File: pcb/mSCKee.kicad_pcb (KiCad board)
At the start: 4 copper layers, 275.3 x 124.4 mm, 192 parts, among them IC1 PCA9956BTWY, IC2 PCA9956BTWY, J2 4P4C, J3 4P4C, J4 USB_C_Receptacle_USB2.0_16P, SW1 SW_Push_45deg, SW10 SW_Push_45deg, SW11 SW_Push_45deg, SW12 SW_Push_45deg, SW13 SW_Push_45deg, SW14 SW_Push_45deg, SW15 SW_Push_45deg, SW16 SW_Push_45deg, SW17 SW_Push_45deg, SW18 SW_Push_45deg, SW19 SW_Push_45deg, SW2 SW_Push_45deg, SW20 SW_Push_45deg, SW21 SW_Push_45deg, SW22 SW_Push_45deg, SW23 SW_Push_45deg, SW24 SW_Push_45deg, SW25 SW_Push_45deg, SW26 SW_Push_45deg, SW27 SW_Push_45deg, SW28 SW_Push_45deg, SW29 SW_Push_45deg, SW3 SW_Push_45deg, SW30 SW_Push_45deg, SW31 SW_Push_45deg, SW32 SW_Push_45deg, SW33 SW_Push_45deg, SW34 SW_Push_45deg, SW35 SW_Push_45deg, SW36 SW_Push_45deg, SW4 SW_Push_45deg, SW5 SW_Push_45deg, SW6 SW_Push_45deg, SW7 SW_Push_45deg, SW8 SW_Push_45deg, SW9 SW_Push_45deg, U1 W25Q128JVSIQ, U2 RP2040, U3 NCP1117LPST33T3G, U4 OPT3001DNPR, U5 NCP1117LPST33T3G, U6 MCP23017T-E/ML, U7 OPT3001DNPR, Y1 ABM8-272-T3

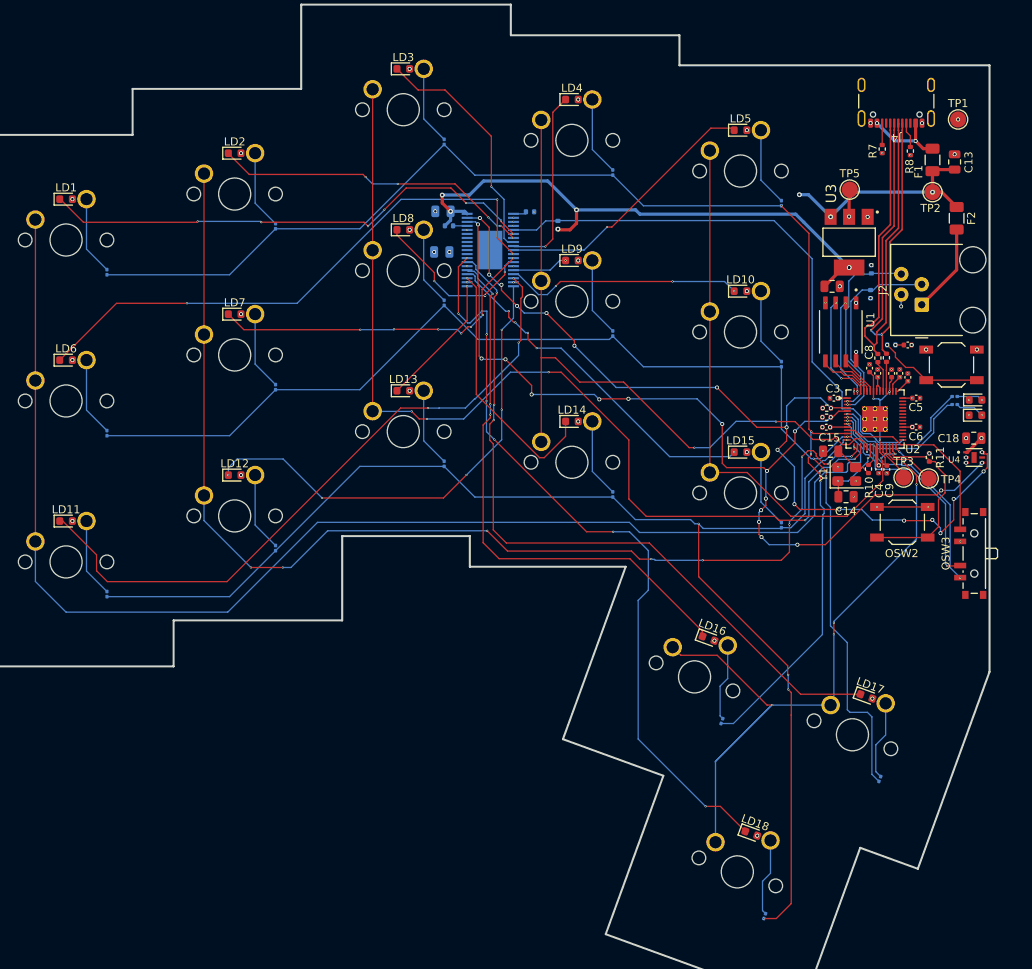
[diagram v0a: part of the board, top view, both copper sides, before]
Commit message: fix: Set all vias to netclass size, fix about half of DRC violations
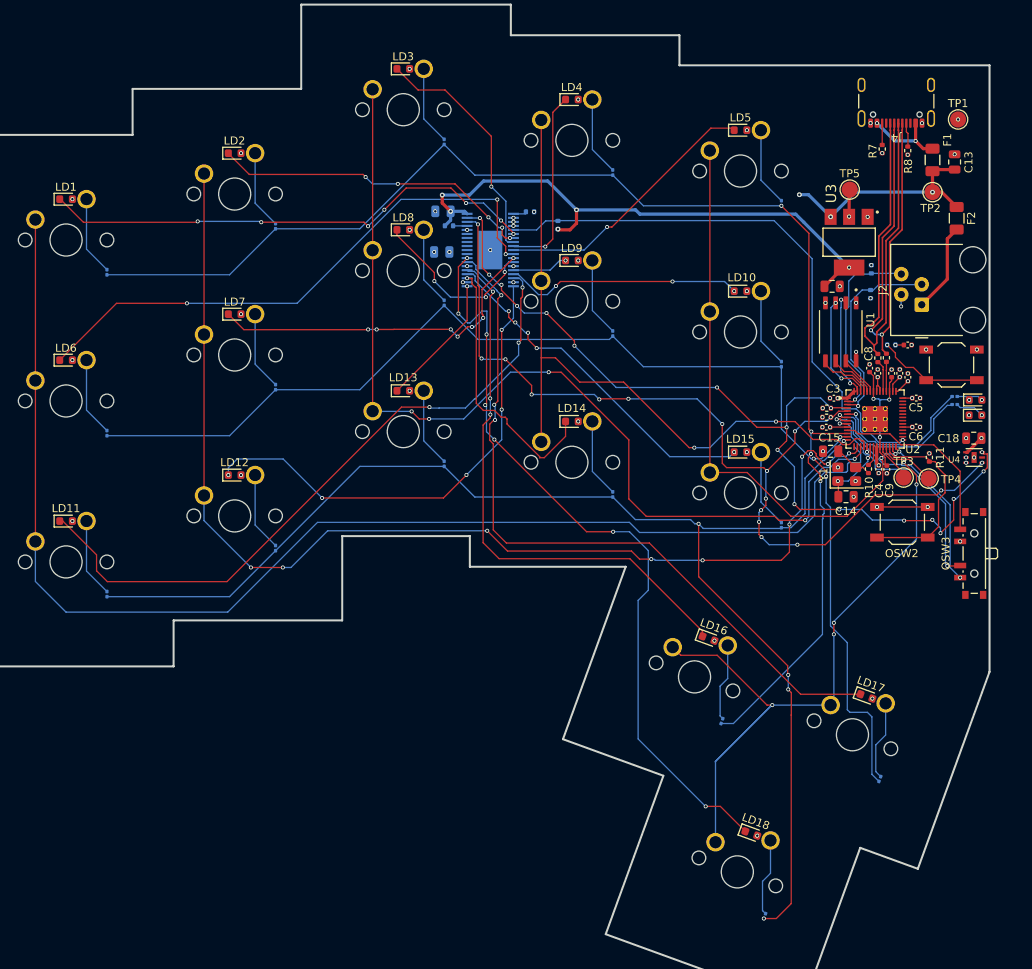
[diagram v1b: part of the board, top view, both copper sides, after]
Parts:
- moved R8 0.33 mm to (188.4, 85.1)
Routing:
- net BL_DIM_1: track 27.5 -> 30.4 mm
- net STATUS2: track 18.7 -> 20.8 mm
- net BL_DIM_2: track 27.5 -> 29.1 mm
- net Net-(IC1-LED13): track 32.2 -> 33.7 mm
- net +3V3: track 94.6 -> 95.7 mm, vias 25 -> 23
- net /master_side/QSPI_SD1: track 12.1 -> 13.3 mm
- net Net-(U2-VREG_VOUT): track 16.4 -> 17.2 mm
- net Net-(IC1-LED16): track 89.8 -> 90.5 mm
- net Net-(IC1-LED6): track 42.4 -> 43.0 mm
- net Net-(IC1-LED5): track 70.3 -> 70.9 mm
- net Net-(IC1-LED10): track 83.2 -> 83.7 mm
- net GND: track 8.45 -> 8.98 mm, vias 48 -> 50
- net Net-(IC1-LED1): track 39.8 -> 40.4 mm
- net Net-(IC1-LED7): track 21.3 -> 21.7 mm, vias 4 -> 3
- net COL0: vias 1 -> 0

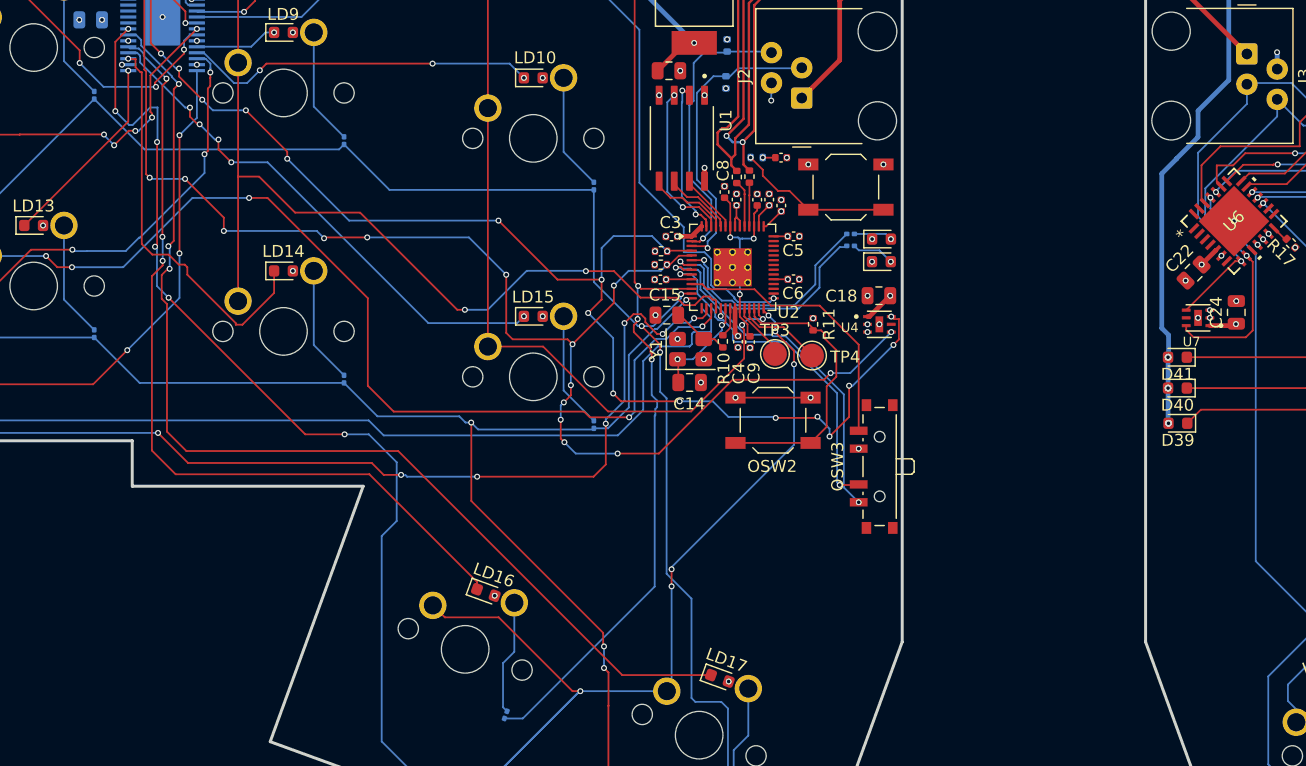
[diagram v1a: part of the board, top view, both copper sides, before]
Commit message: fix: DRC violations, 0 errors, about 70 silkscreen warnings remain
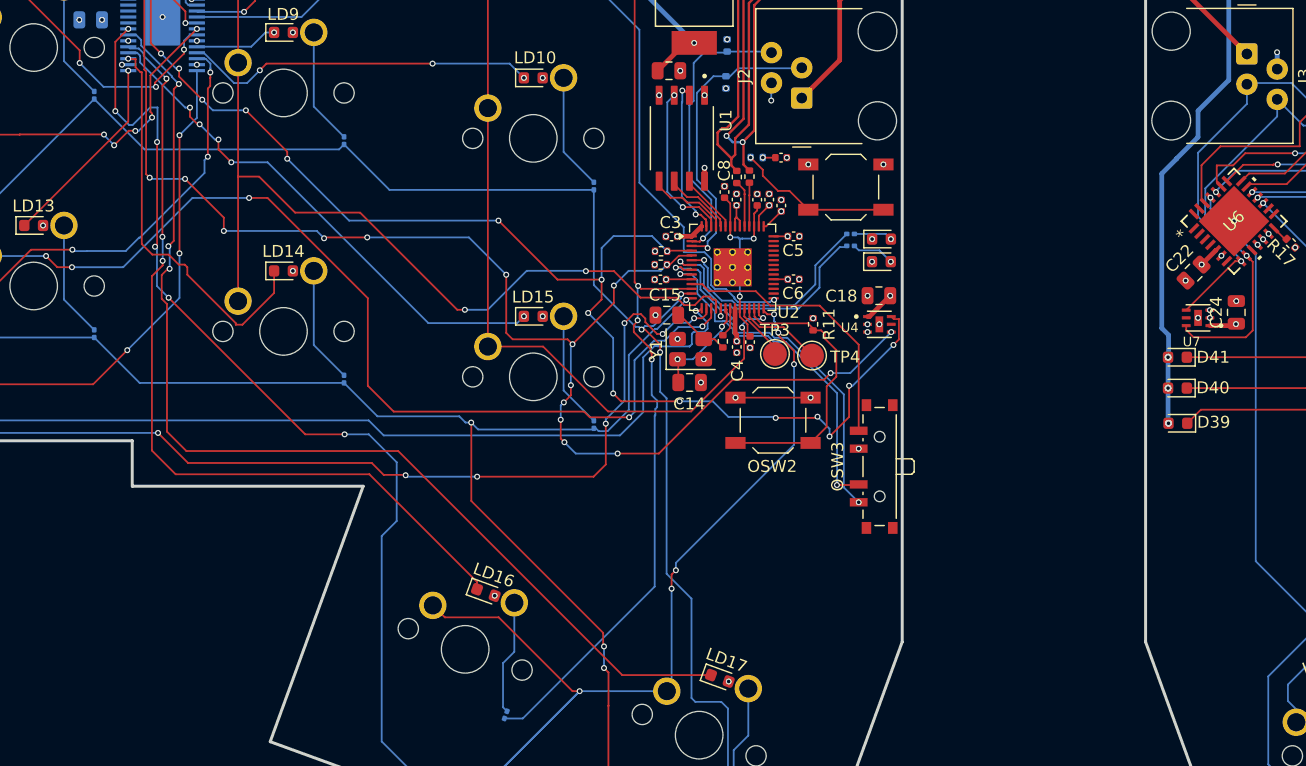
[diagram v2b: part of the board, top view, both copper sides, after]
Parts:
- moved C4 0.45 mm to (184.7, 125.1)
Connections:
- C25 pad 2: unconnected-(C25-Pad2) -> R_GND
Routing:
- net BL_DIM_1: track 30.4 -> 31.0 mm
- net COL0: track 163.1 -> 163.4 mm, vias 0 -> 1
- net unconnected-(C25-Pad2): vias 1 -> 0
- net R_GND: vias 24 -> 25
- net I2C_D: vias 18 -> 17

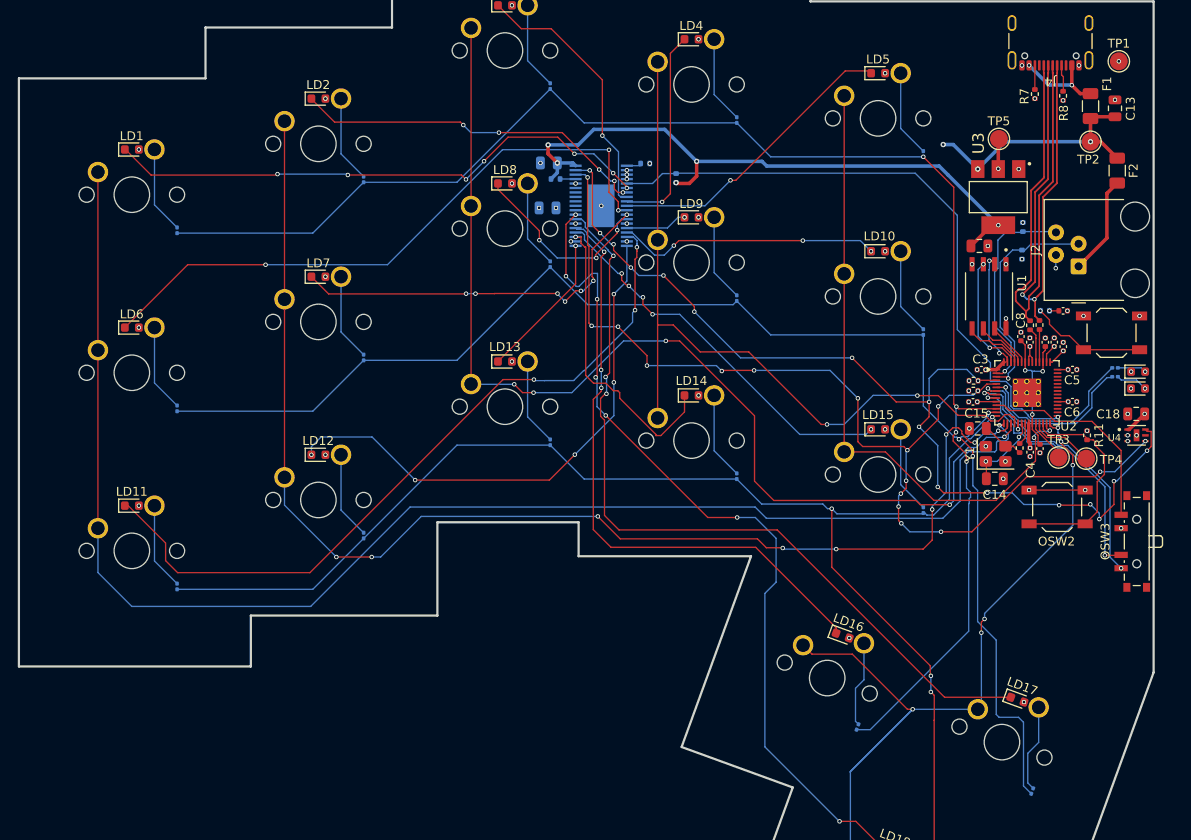
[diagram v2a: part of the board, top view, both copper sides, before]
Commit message: feat(left side): Add 5 mounting holes
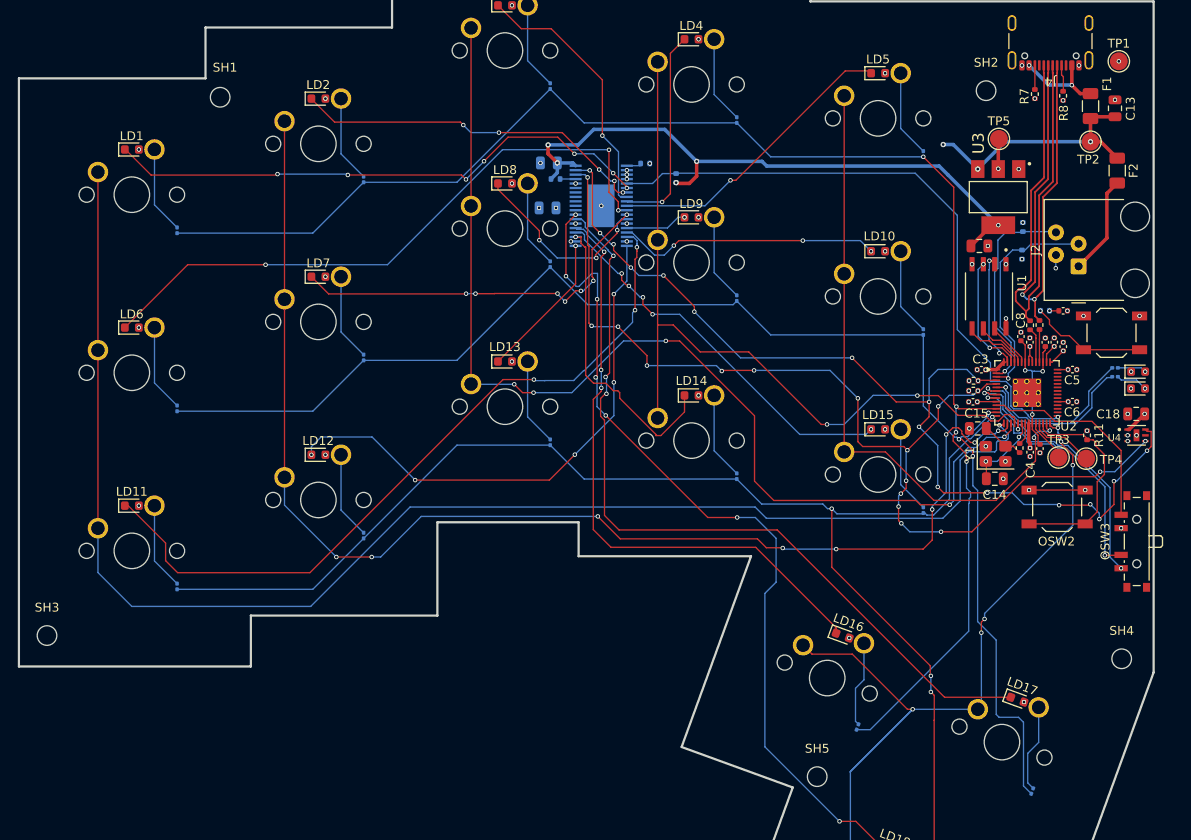
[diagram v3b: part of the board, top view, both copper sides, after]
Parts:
- added SH1: MountingHole_2.2mm_M2, MountingHole:MountingHole_2.2mm_M2, F.Cu at (93.7, 85.3)
- added SH2: MountingHole_2.2mm_M2, MountingHole:MountingHole_2.2mm_M2, F.Cu at (179.8, 84.5)
- added SH3: MountingHole_2.2mm_M2, MountingHole:MountingHole_2.2mm_M2, F.Cu at (74.3, 145.7)
- added SH4: MountingHole_2.2mm_M2, MountingHole:MountingHole_2.2mm_M2, F.Cu at (195.0, 148.3)
- added SH5: MountingHole_2.2mm_M2, MountingHole:MountingHole_2.2mm_M2, F.Cu at (160.8, 161.6)

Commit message: feat: Set grid origin to exactly center between the halves, add mounting holes to both sides and align them
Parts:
- added SH10: MountingHole_2.2mm_M2, MountingHole:MountingHole_2.2mm_M2, F.Cu at (343.3, 145.7)
- added SH6: MountingHole_2.2mm_M2, MountingHole:MountingHole_2.2mm_M2, F.Cu at (222.6, 148.3)
- added SH7: MountingHole_2.2mm_M2, MountingHole:MountingHole_2.2mm_M2, F.Cu at (256.8, 161.6)
- added SH8: MountingHole_2.2mm_M2, MountingHole:MountingHole_2.2mm_M2, F.Cu at (237.8, 84.5)
- added SH9: MountingHole_2.2mm_M2, MountingHole:MountingHole_2.2mm_M2, F.Cu at (323.8, 85.3)
- moved C21 3.54 mm to (239.4, 89.9), turned to 90 degrees
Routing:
- net +3V3_R: track 61.9 -> 63.6 mm, vias 9 -> 8
